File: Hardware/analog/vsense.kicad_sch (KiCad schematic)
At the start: 20 parts

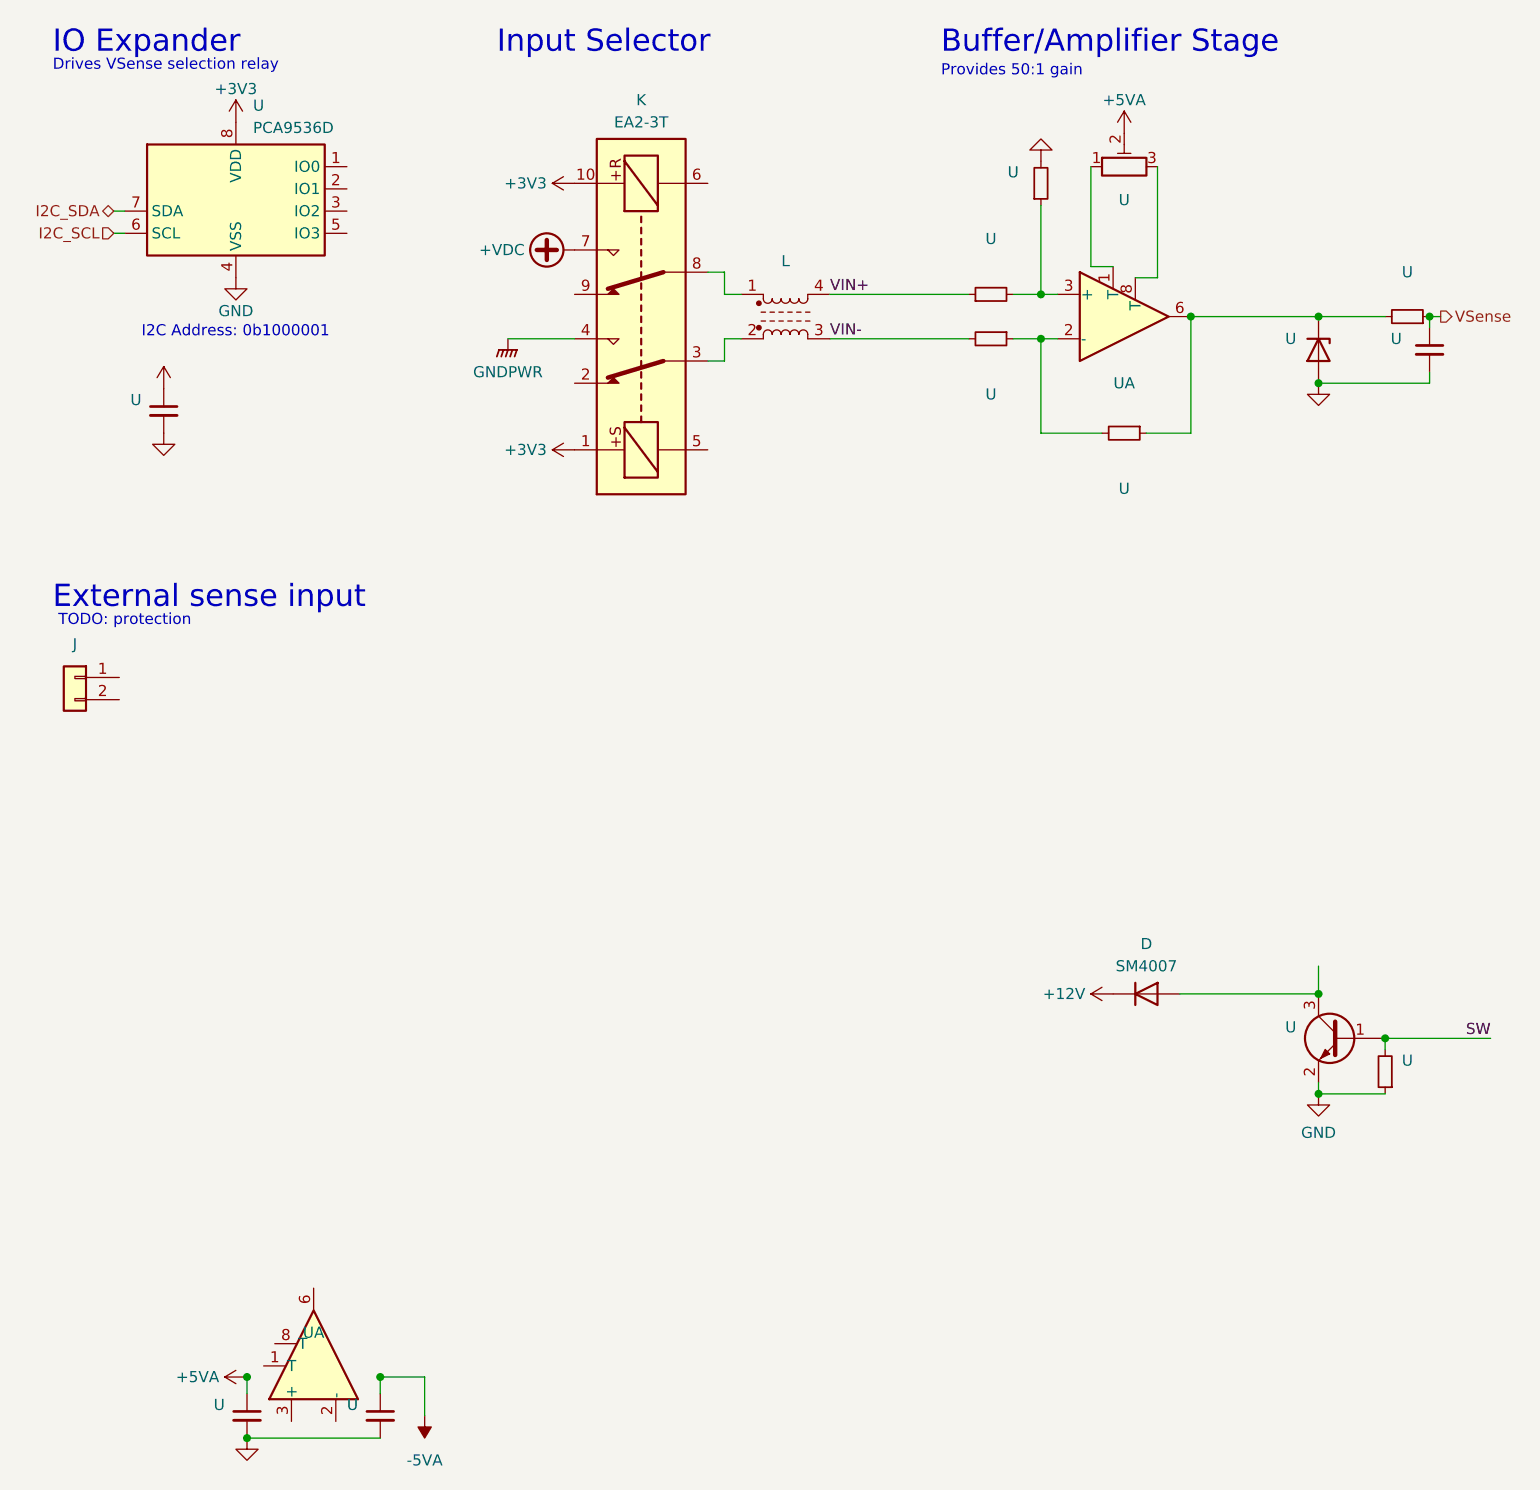
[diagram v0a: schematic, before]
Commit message: Mostly finished up analog load board
- Finished routing most signals

- Connected relay drive to bonus I2C GPIO controller, and routed the
  rest of the voltage sense stuff

- Routed the reset signal to the DAC, so that when the board is reset,
  the current output will be reset to zero as well without processor
  intervention

- Replaced most passives with 0603/1608 size
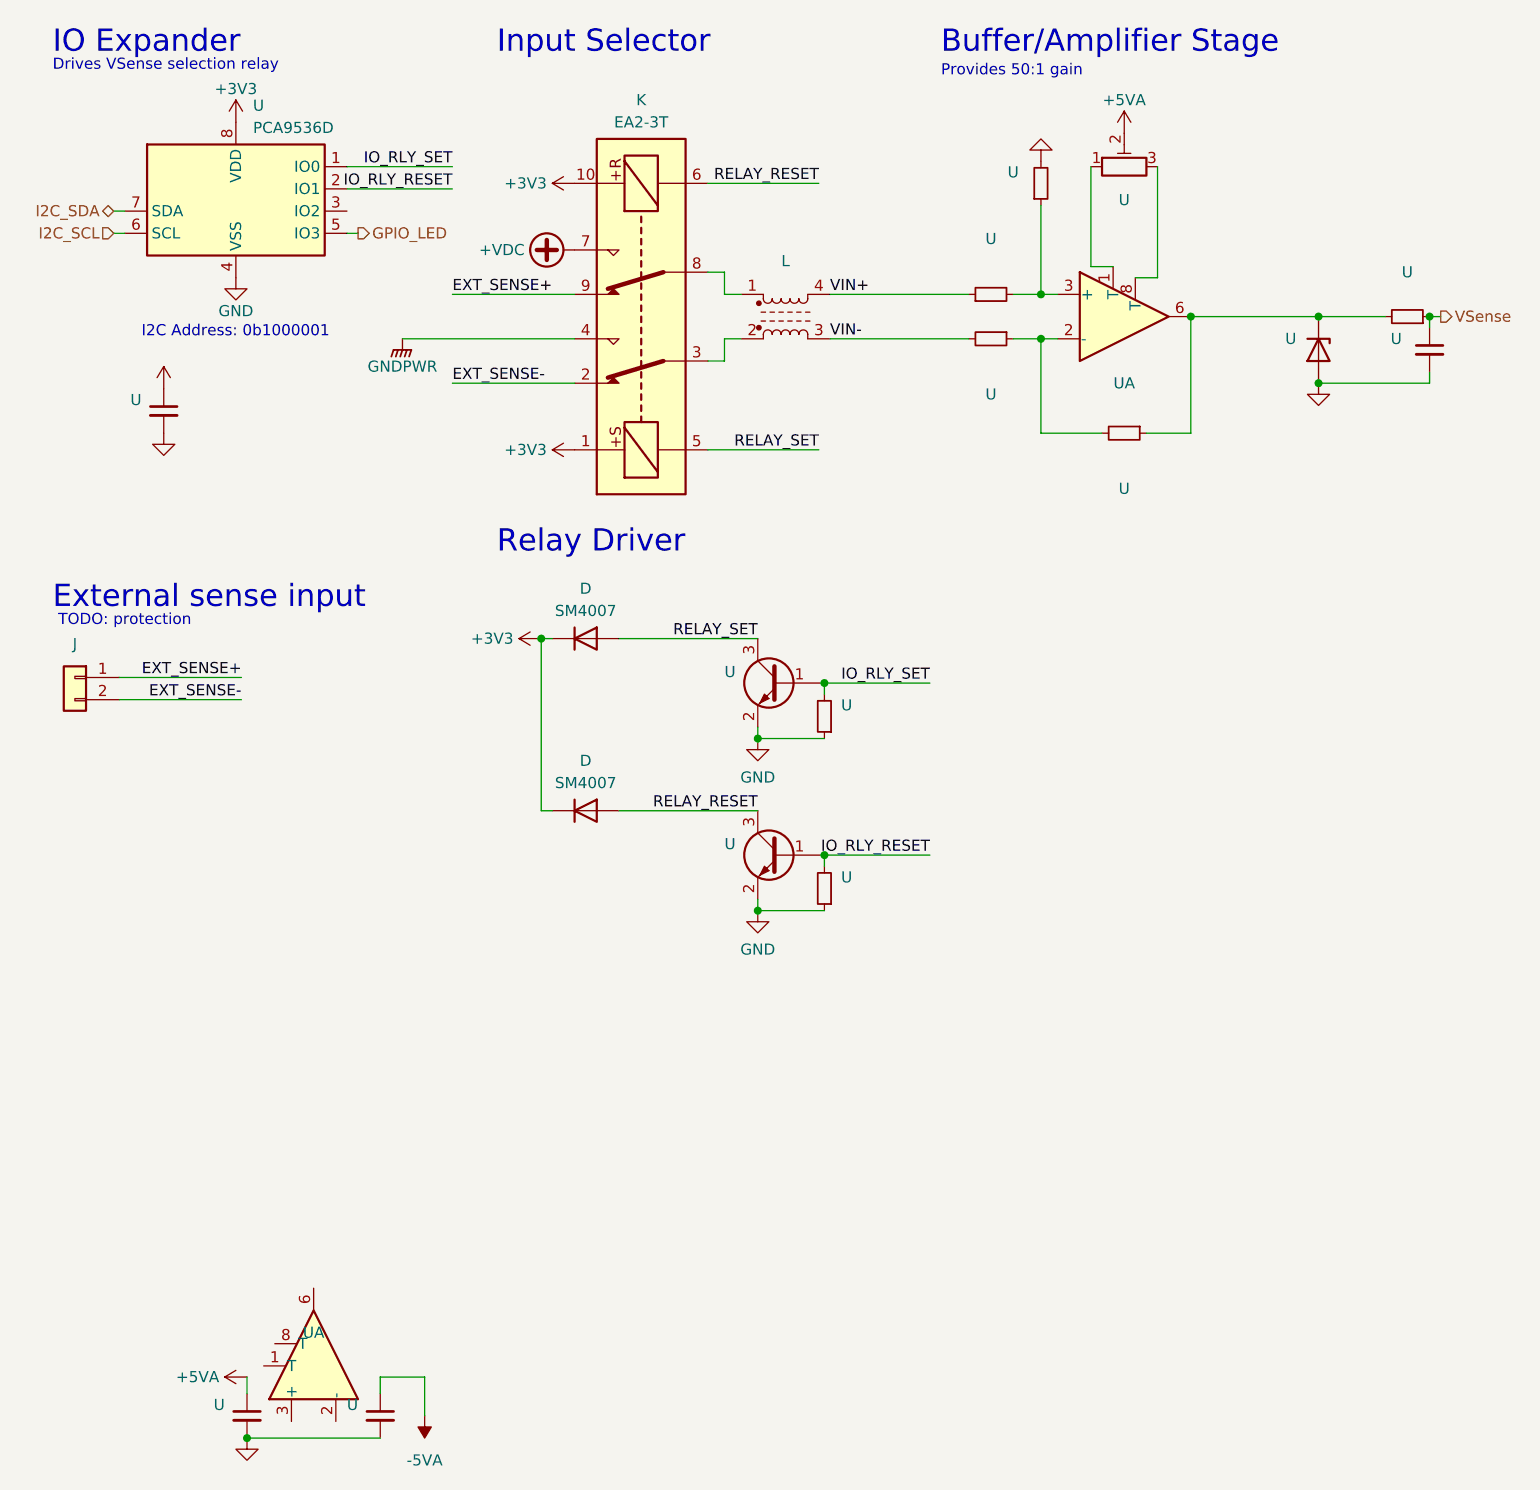
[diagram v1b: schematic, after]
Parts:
- added D: SM4007, Diode_SMD:D_MELF, symbol Diode:SM4007
- added U: (no value), symbol Transistor_BJT:MMBT3904
- added U: (no value), symbol Device:R_Small
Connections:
- net +12V is gone; now on net +3V3: D.1 (K)
- net SW is gone; now on net IO_RLY_SET: U.1 (B), U.2
- net +3V3: now also D.1 (K)
- net GND: now also U.1, U.2 (E)
- net EXT_SENSE-: now reaches K.2
- net EXT_SENSE-: now also J.2 (Pin_2)
- net RELAY_SET: now reaches K.5
- net RELAY_SET: now also D.2 (A), U.3 (C)
- net RELAY_RESET: now reaches K.6
- net RELAY_RESET: now also D.2 (A), U.3 (C)
- net EXT_SENSE+: now reaches K.9
- net EXT_SENSE+: now also J.1 (Pin_1)
- net IO_RLY_SET: now reaches U.1 (IO0)
- net IO_RLY_RESET: now reaches U.2 (IO1)
- net IO_RLY_RESET: now also U.1 (B), U.2
- net GPIO_LED: now reaches U.5 (IO3)
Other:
- note added: "Relay Driver"
- moved on the sheet: D, U

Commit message: Temperature sensing & cleanup for analog board
- Added the auxiliary temperature sensing ADC, and routed it to the
  analog temperature sensors on the front and rear of the MOSFET
  heatsink

- Added an LM75 sensor to measure the analog board ambient temperature
  (for better temperature control/fan control)

  This may end up being a DNP item if it's not really useful or
  otherwise necessary.

- Fixes to a few symbols (namely pin directions) to pass ERC
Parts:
- added D: D_TVS, symbol Device:D_TVS
- added D: D_Schottky_Small, symbol Device:D_Schottky_Small
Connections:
- net EXT_SENSE+: now also D.1 (K); no longer J.1 (Pin_1)
- net EXT_SENSE-: now also D.1 (A1)
- new net: D.2 (A), D.2 (A2), J.1 (Pin_1)
- no-connect marks 0 -> 1
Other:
- note removed: "TODO: protection"
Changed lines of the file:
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@@
   (junction (at 74.93 85.725) (diameter 0) (color 0 0 0 0)
   )
+  (junction (at 45.085 90.17) (diameter 0) (color 0 0 0 0)
+  )
   (junction (at 149.225 48.895) (diameter 0) (color 0 0 0 0)
   )
@@
   (junction (at 132.08 51.435) (diameter 0) (color 0 0 0 0)
   )
+  (no_connect (at 52.705 36.83))
+  (wire (pts (xy 45.085 102.235) (xy 45.085 103.505))
+    (stroke (width 0) (type default))
+  )
   (wire (pts (xy 107.315 110.49) (xy 119.38 110.49))
     (stroke (width 0) (type default))
   )
+  (wire (pts (xy 45.085 90.17) (xy 47.625 90.17))
+    (stroke (width 0) (type default))
+  )
   (wire (pts (xy 74.93 85.725) (xy 74.93 105.41))
     (stroke (width 0) (type default))
@@
     (stroke (width 0) (type default))
   )
-  (wire (pts (xy 40.64 90.17) (xy 26.67 90.17))
+  (wire (pts (xy 26.67 90.17) (xy 45.085 90.17))
     (stroke (width 0) (type default))
   )
@@
     (stroke (width 0) (type default))
   )
+  (wire (pts (xy 45.085 90.17) (xy 45.085 94.615))
+    (stroke (width 0) (type default))
+  )
   (wire (pts (xy 144.145 62.23) (xy 149.225 62.23))
     (stroke (width 0) (type default))
   )
+  (wire (pts (xy 66.675 90.17) (xy 52.705 90.17))
+    (stroke (width 0) (type default))
+  )
+  (wire (pts (xy 40.64 103.505) (xy 40.64 92.71))
+    (stroke (width 0) (type default))
+  )
   (wire (pts (xy 93.98 64.135) (xy 106.68 64.135))
     (stroke (width 0) (type default))
@@
   )
   (wire (pts (xy 99.695 116.84) (xy 99.695 115.57))
+    (stroke (width 0) (type default))
+  )
+  (wire (pts (xy 45.085 103.505) (xy 40.64 103.505))
     (stroke (width 0) (type default))
   )
@@
     (effects (font (size 1.27 1.27)) (justify left bottom))
   )
-  (text "TODO: protection" (at 19.685 84.455 0)
-    (effects (font (size 1.27 1.27)) (justify left bottom))
-  )
   (text "Drives VSense selection relay" (at 19.05 20.955 0)
     (effects (font (size 1.27 1.27)) (justify left bottom))
@@
     (effects (font (size 1.27 1.27)) (justify left bottom))
   )
-  (label "EXT_SENSE+" (at 40.64 90.17 0) (fields_autoplaced)
+  (label "EXT_SENSE+" (at 66.675 90.17 0) (fields_autoplaced)
     (effects (font (size 1.27 1.27)) (justify right bottom))
   )
@@
     (pin "2")
   )
+  (symbol (lib_id "Device:D_TVS") (at 45.085 98.425 90) (unit 1)
+    (in_bom yes) (on_board yes) (fields_autoplaced)
+    (default_instance (reference "D") (unit 1) (value "D_TVS") (footprint ""))
+    (property "Reference" "D" (id 0) (at 48.26 97.79 90)
+      (effects (font (size 1.27 1.27)) (justify right))
+    )
+    (property "Value" "D_TVS" (id 1) (at 48.26 100.33 90)
+      (effects (font (size 1.27 1.27)) (justify right))
+    )
+    (property "Footprint" "" (id 2) (at 45.085 98.425 0)
+      (effects (font (size 1.27 1.27)) hide)
+    )
+    (property "Datasheet" "~" (id 3) (at 45.085 98.425 0)
+      (effects (font (size 1.27 1.27)) hide)
+    )
+    (property "MPN" "824501751" (id 4) (at 45.085 98.425 90)
+      (effects (font (size 1.27 1.27)) hide)
+    )
+    (pin "1")
+    (pin "2")
+  )
   (symbol (lib_id "Device:R_Potentiometer_Trim") (at 141.605 31.75 90) (unit 1)
     (in_bom yes) (on_board yes) (fields_autoplaced)
@@
     (pin "3")
   )
+  (symbol (lib_id "Device:D_Schottky_Small") (at 50.165 90.17 180) (unit 1)
+    (in_bom yes) (on_board yes) (fields_autoplaced)
+    (default_instance (reference "D") (unit 1) (value "D_Schottky_Small") (footprint ""))
+    (property "Reference" "D" (id 0) (at 50.419 85.09 0)
+      (effects (font (size 1.27 1.27)))
+    )
+    (property "Value" "D_Schottky_Small" (id 1) (at 50.419 87.63 0)
+      (effects (font (size 1.27 1.27)))
+    )
+    (property "Footprint" "" (id 2) (at 50.165 90.17 90)
+      (effects (font (size 1.27 1.27)) hide)
+    )
+    (property "Datasheet" "~" (id 3) (at 50.165 90.17 90)
+      (effects (font (size 1.27 1.27)) hide)
+    )
+    (property "MPN" "SS110-HF" (id 4) (at 50.165 90.17 0)
+      (effects (font (size 1.27 1.27)) hide)
+    )
+    (pin "1")
+    (pin "2")
+  )
   (symbol (lib_id "power:+5VA") (at 41.275 170.18 90) (unit 1)
